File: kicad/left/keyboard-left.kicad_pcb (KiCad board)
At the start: 2 copper layers, 163 x 121 mm, 90 parts, among them J1 USB_C_Receptacle_USB2.0_14P, J2 AudioJack4, J3 Conn_01x04_Pin, SW1 SW_Push, SW10 SW_Push, SW11 SW_Push, SW12 SW_Push, SW13 SW_Push, SW14 SW_Push, SW15 SW_Push, SW16 SW_Push, SW17 SW_Push, SW18 SW_Push, SW19 SW_Push, SW2 SW_Push, SW20 SW_Push, SW21 SW_Push, SW22 SW_Push, SW23 SW_Push, SW24 SW_Push, SW25 SW_Push, SW26 SW_Push, SW27 SW_Push, SW28 SW_Push, SW29 SW_Push, SW3 SW_Push, SW30 SW_Push, SW31 SW_Push, SW32 SW_Push, SW33 SW_Push, SW34 SW_Push, SW35 SW_Push, SW4 SW_Push, SW5 SW_Push, SW6 SW_Push, SW7 SW_Push, SW8 SW_Push, SW9 SW_Push, U1 AVR32DU32x-xPT

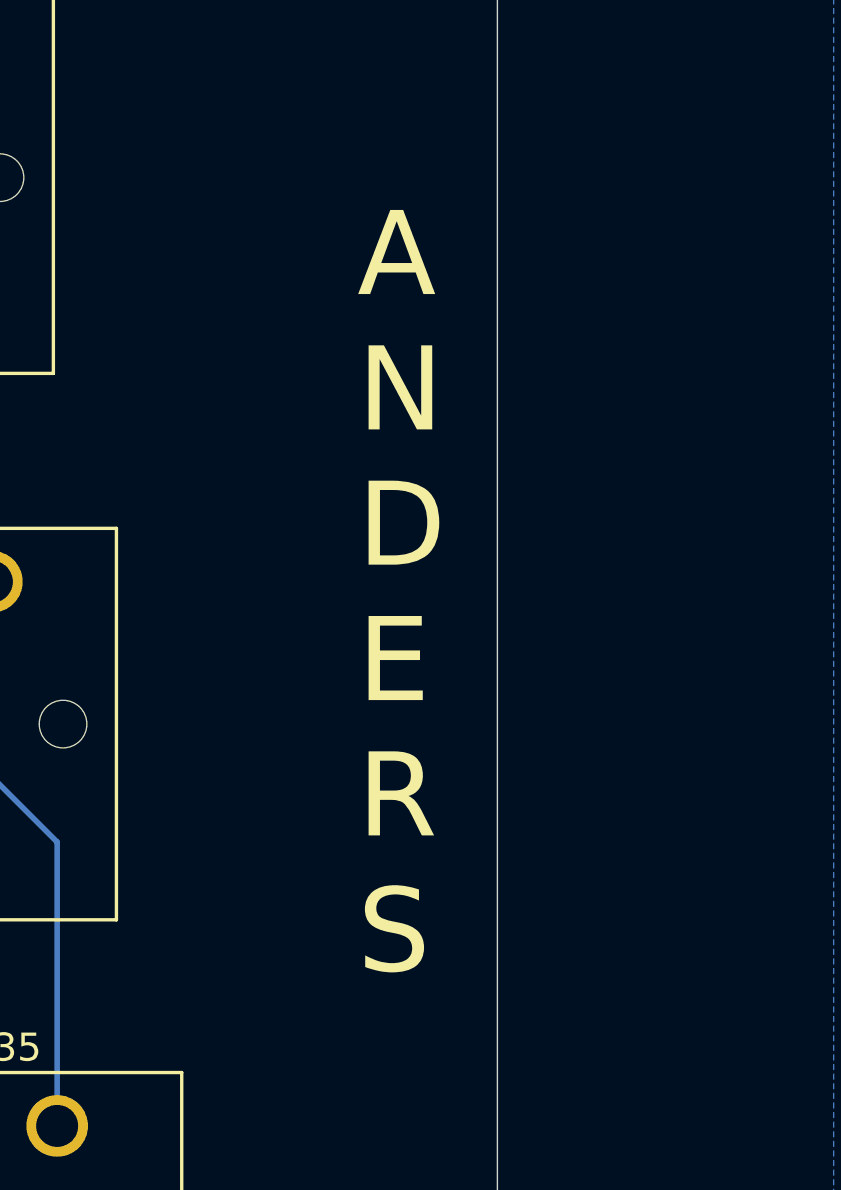
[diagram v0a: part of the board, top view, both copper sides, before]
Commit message: finished up right side pcb
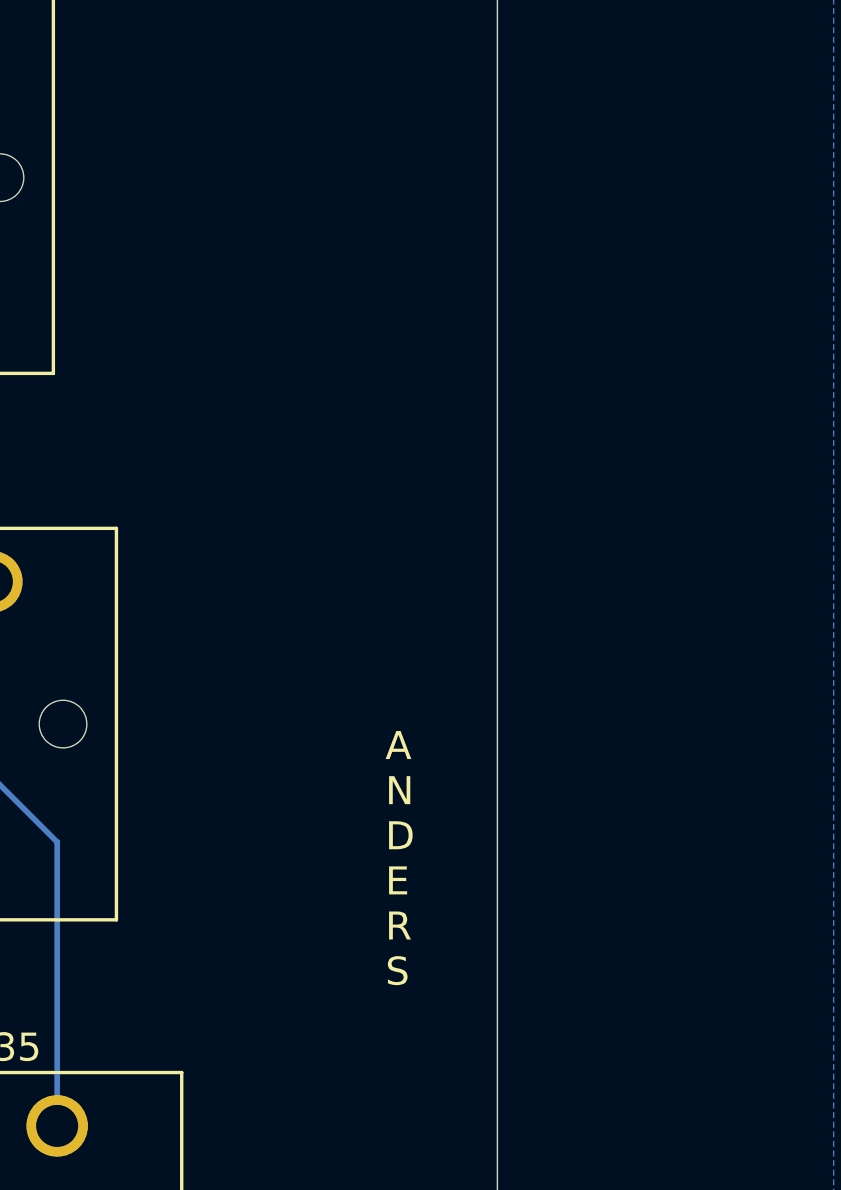
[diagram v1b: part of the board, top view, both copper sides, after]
